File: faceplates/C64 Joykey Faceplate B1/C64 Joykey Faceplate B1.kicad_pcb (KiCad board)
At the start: 2 copper layers, 99.7 x 74.9 mm, 5 parts, among them M1 Mounting, M2 Mounting, M3 Mounting, M4 Mounting

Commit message: Blank B1
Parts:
- removed G***: LOGO, artwork:robocop
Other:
- outline, holes or cut-outs redrawn

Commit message: Play around with graphics
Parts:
- added G***: LOGO, artwork:platoon, F.Cu at (189.1, 112.8)

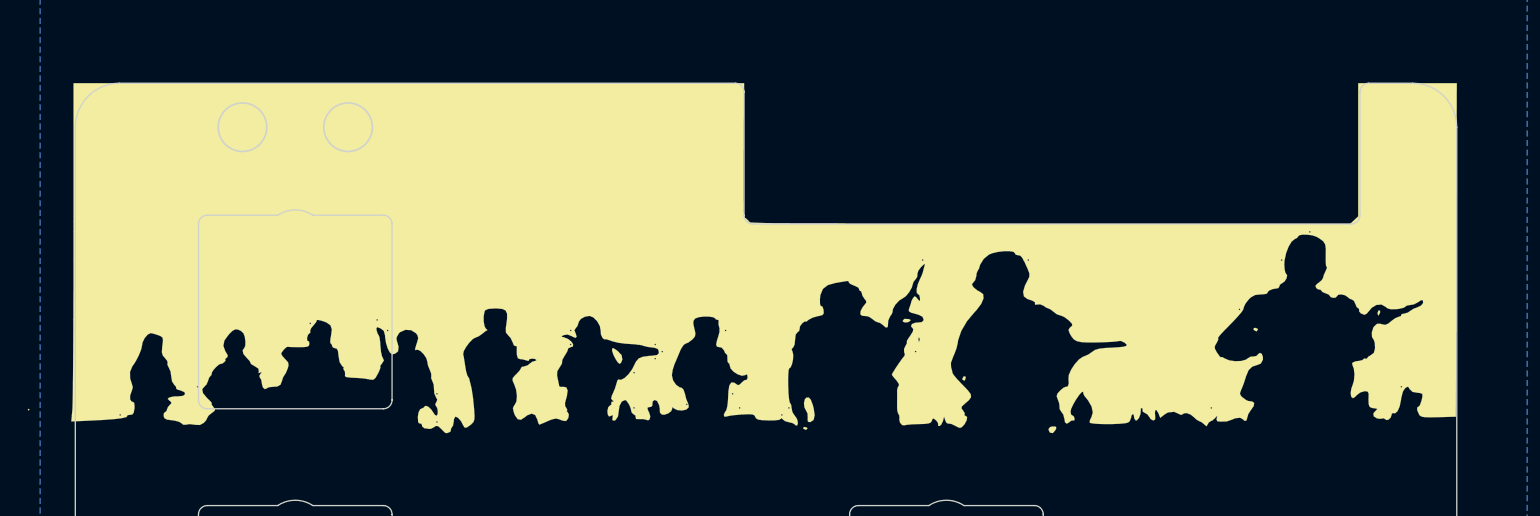
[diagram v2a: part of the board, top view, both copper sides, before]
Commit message: Tweaked faceplates to allow more leeway on LEDs
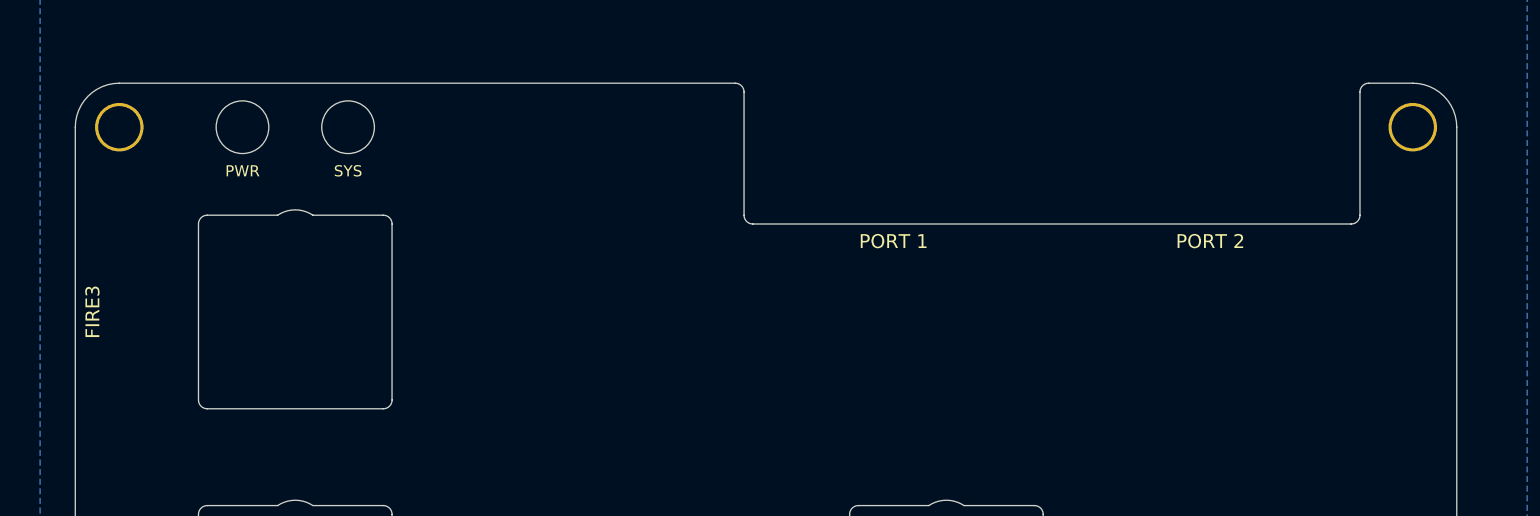
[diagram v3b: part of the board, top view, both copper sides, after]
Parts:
- removed G***: LOGO, artwork:platoon
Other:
- outline, holes or cut-outs redrawn
